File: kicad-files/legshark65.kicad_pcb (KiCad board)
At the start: 2 copper layers, 290 x 92 mm, 158 parts, among them SW1 K2-1187SQ-A4SW-06, SW2 PCM12SMTR, T2 53261-0471, U1 STM32F411CEU6, U3 AT24C256C-SSHL-T, Y1 TAXM8M4RFDCET2T

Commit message: Finished wiring the board
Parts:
- removed SWD1: ~, Legshark:1x02_Long_Header
- added J1: ARM JTAG, acheron_Connectors:PinHeader_2x5_P2.54mm_Vertical, B.Cu at (291.1, 87.4)
- moved Legshark_Logo2 158.7 mm to (83.8, 70.0), turned to -16 degrees
- moved C10 1.63 mm to (259.8, 72.5)
- moved C15 1.60 mm to (246.9, 86.0)
- moved C16 1.27 mm to (246.9, 98.6)
- moved C13 1.21 mm to (261.1, 94.8), turned to 180 degrees
- moved C12 1.11 mm to (261.1, 92.8), turned to 180 degrees
- moved R6 0.54 mm to (246.9, 88.7), turned to 90 degrees
- moved R1 0.15 mm to (247.5, 75.5)
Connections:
- net Net-(U1-BOOT0) renamed BOOT0
- net Net-(U1-NRST) renamed NRST
- net Net-(U1-PB2--BOOT1) renamed BOOT1
- U1 pad 34: Net-(SWD1-SWDIO) -> SWDIO
- U1 pad 37: Net-(SWD1-SWCLK) -> SWCLK
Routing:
- net SWDIO: track 0.00 -> 58.5 mm, vias 0 -> 1
- net BOOT1: track 6.01 -> 62.3 mm, vias 0 -> 1
- net SWCLK: track 0.00 -> 50.7 mm, vias 0 -> 1
- net 3V3: track 88.2 -> 128.9 mm
- net BOOT0: track 28.0 -> 55.2 mm, vias 0 -> 2
- net Net-(SWD1-SWCLK): track 24.7 -> 0.00 mm
- net NRST: track 27.7 -> 47.6 mm, vias 2 -> 3
- net Net-(SWD1-SWDIO): track 19.1 -> 0.00 mm
- net c14: track 100.6 -> 118.6 mm
- net c13: track 89.8 -> 93.4 mm, vias 1 -> 3
- net r4: track 281.7 -> 285.0 mm
- net GND: track 20.5 -> 23.5 mm, vias 12 -> 20
- net c12: track 76.0 -> 78.5 mm
- net c11: track 96.2 -> 98.5 mm
- net c6: track 231.3 -> 229.9 mm
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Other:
- board size 290 x 92 mm -> 286 x 96 mm
- board text added: "3V3"
- board text added: "BOOT0"
- board text added: "BOOT1"
- board text added: "GND"
- board text added: "JTAG"
- board text added: "Reset"
- board text added: "SWCLK"
- board text added: "SWDIO"
- board text added: "nRST"

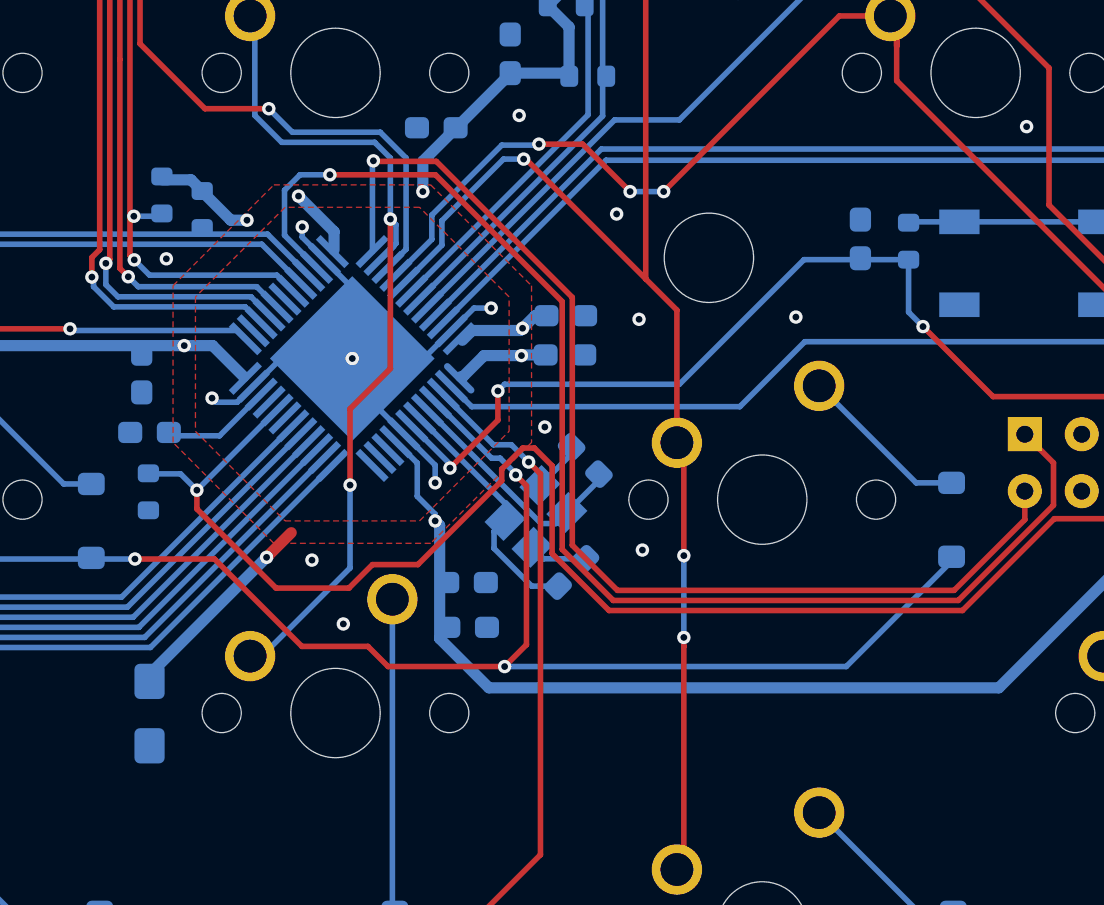
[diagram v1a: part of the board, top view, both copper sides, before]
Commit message: Added names to molex connector
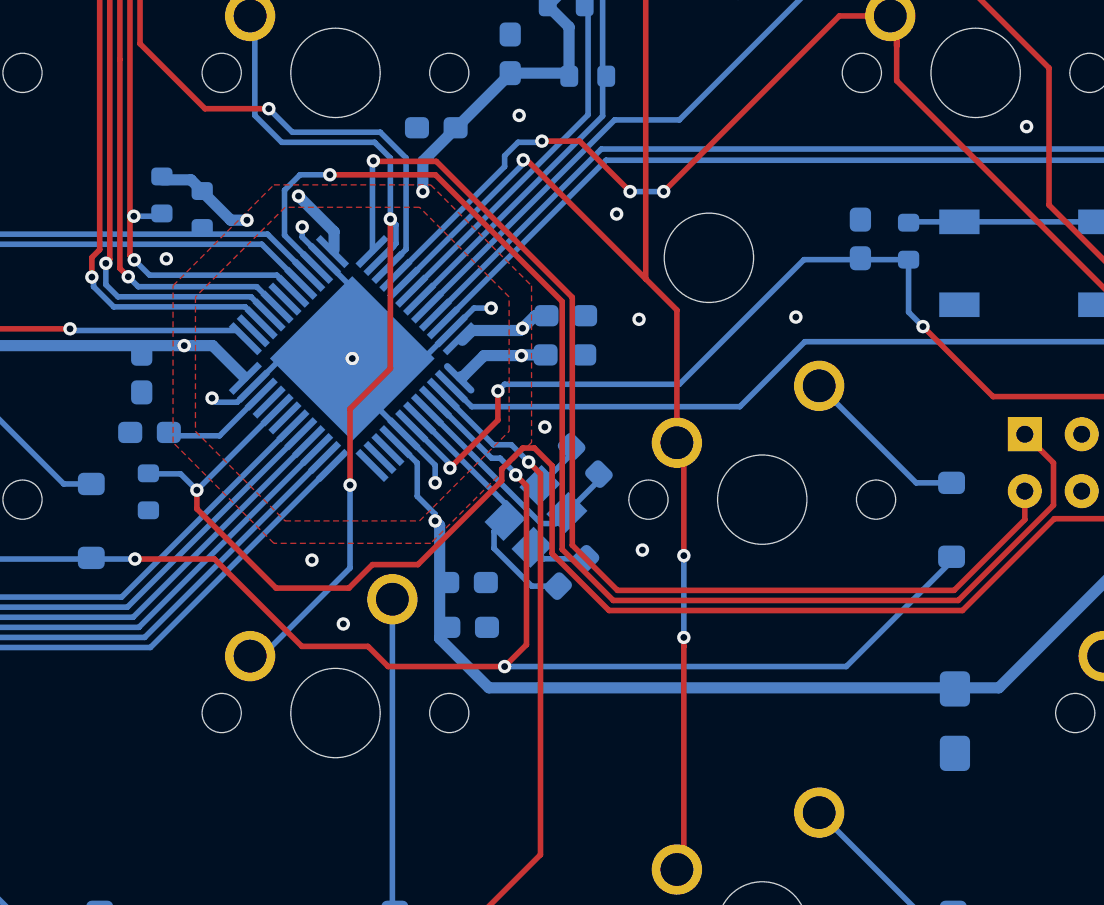
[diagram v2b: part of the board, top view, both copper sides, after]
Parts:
- moved C16 36.0 mm to (282.9, 98.9)
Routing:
- net 3V3: track 128.9 -> 119.6 mm, vias 8 -> 7
- net c13: track 93.4 -> 92.9 mm
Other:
- board text added: "D+"
- board text added: "D-"
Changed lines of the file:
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@@
   )
   (footprint "acheron_Components:CP_EIA-3216-10_Kemet-I_Pad1.58x1.35mm_HandSolder" (layer "B.Cu")
-    (at 246.95 98.6 -90)
+    (at 282.9 98.9375 -90)
     (descr "Tantalum Capacitor SMD Kemet-I (3216-10 Metric), IPC_7351 nominal, (Body size from: http://www.kemet.com/Lists/ProductCatalog/Attachments/253/KEM_TC101_STD.pdf), generated with kicad-footprint-generator")
     (tags "capacitor tantalum")
@@
     (effects (font (size 0.8 0.8) (thickness 0.16)) (justify right mirror))
   )
+  (gr_text "D-" (at 231.3 81) (layer "B.SilkS")
+    (effects (font (size 0.8 0.8) (thickness 0.16)) (justify right mirror))
+  )
   (gr_text "SWCLK" (at 286.02 89.94 90) (layer "B.SilkS")
     (effects (font (size 0.8 0.8) (thickness 0.16)) (justify left mirror))
@@
     (effects (font (size 0.8 0.8) (thickness 0.16)) (justify right mirror))
   )
+  (gr_text "D+" (at 231.3 79.7) (layer "B.SilkS")
+    (effects (font (size 0.8 0.8) (thickness 0.16)) (justify right mirror))
+  )
   (gr_text "3V3" (at 293.64 89.94 90) (layer "B.SilkS")
     (effects (font (size 0.8 0.8) (thickness 0.16)) (justify left mirror))
@@
     (effects (font (size 0.8 0.8) (thickness 0.16)) (justify right mirror))
   )
+  (gr_text "3V3" (at 231.3 82.2) (layer "B.SilkS")
+    (effects (font (size 0.8 0.8) (thickness 0.16)) (justify right mirror))
+  )
   (gr_text "BOOT1" (at 291.1 89.94 90) (layer "B.SilkS")
     (effects (font (size 0.8 0.8) (thickness 0.16)) (justify left mirror))
   )
+  (gr_text "GND" (at 231.3 78.4) (layer "B.SilkS")
+    (effects (font (size 0.8 0.8) (thickness 0.16)) (justify right mirror))
+  )
   (gr_text "GND" (at 296.18 89.94 90) (layer "B.SilkS")
     (effects (font (size 0.8 0.8) (thickness 0.16)) (justify left mirror))
@@
   (segment (start 265.083883 90.118198) (end 265.578858 89.623223) (width 0.25) (layer "B.Cu") (net 3))
   (segment (start 259.358757 85.048097) (end 264.428858 90.118198) (width 0.25) (layer "B.Cu") (net 3))
-  (segment (start 252.175 91.625) (end 253.275 90.525) (width 0.5) (layer "F.Cu") (net 4))
   (via (at 263.6 81.4) (size 0.6) (drill 0.3) (layers "F.Cu" "B.Cu") (net 4))
   (via (at 259.15 75.3) (size 0.6) (drill 0.3) (layers "F.Cu" "B.Cu") (net 4))
@@
   (via (at 259.7 90) (size 0.6) (drill 0.3) (layers "F.Cu" "B.Cu") (net 4))
   (via (at 253.6 75.5) (size 0.6) (drill 0.3) (layers "F.Cu" "B.Cu") (net 4))
-  (via (at 252.175 91.625) (size 0.6) (drill 0.3) (layers "F.Cu" "B.Cu") (net 4))
   (segment (start 263.55 82.62) (end 261.88 82.62) (width 0.5) (layer "B.Cu") (net 4))
   (segment (start 274.1 61.5) (end 277.5 61.5) (width 0.5) (layer "B.Cu") (net 4))
@@
   (segment (start 259.15 75.3) (end 259.15 73.943146) (width 0.5) (layer "B.Cu") (net 4))
   (segment (start 260.936828 83.563172) (end 260.843682 83.563172) (width 0.5) (layer "B.Cu") (net 4))
-  (segment (start 252.175 91.625) (end 246.95 96.85) (width 0.5) (layer "B.Cu") (net 4))
   (segment (start 263.6 81.4) (end 263.5 81.5) (width 0.5) (layer "B.Cu") (net 4))
   (segment (start 255.186828 77.086828) (end 255.186828 77.906318) (width 0.5) (layer "B.Cu") (net 4))
@@
   (segment (start 293.64 88.67) (end 293.64 86.13) (width 0.5) (layer "B.Cu") (net 4))
   (segment (start 269.1 61.9) (end 270.4 60.6) (width 0.5) (layer "B.Cu") (net 4))
-  (segment (start 246.95 96.85) (end 246.95 97.1625) (width 0.5) (layer "B.Cu") (net 4))
   (segment (start 261.88 82.62) (end 260.936828 83.563172) (width 0.5) (layer "B.Cu") (net 4))
   (segment (start 249.3 75.275) (end 248.8 74.775) (width 0.5) (layer "B.Cu") (net 4))
@@
   (segment (start 257.951345 76.77819) (end 257.951345 77.616675) (width 0.25) (layer "B.Cu") (net 88))
   (segment (start 270.8 95.6) (end 270.8 105.25) (width 0.25) (layer "F.Cu") (net 89))
-  (segment (start 263.7495 73.8495) (end 269.1 79.2) (width 0.25) (layer "F.Cu") (net 89))
   (segment (start 270.8 86.82) (end 270.49 86.51) (width 0.25) (layer "F.Cu") (net 89))
+  (segment (start 263.628317 73.884951) (end 263.784951 73.884951) (width 0.25) (layer "F.Cu") (net 89))
+  (segment (start 263.784951 73.884951) (end 269.1 79.2) (width 0.25) (layer "F.Cu") (net 89))
   (segment (start 270.7 60.2) (end 269.1 61.8) (width 0.25) (layer "F.Cu") (net 89))
   (segment (start 270.7 29.57) (end 270.7 60.2) (width 0.25) (layer "F.Cu") (net 89))
   (segment (start 270.49 80.59) (end 270.49 86.51) (width 0.25) (layer "F.Cu") (net 89))
-  (segment (start 263.65 73.8495) (end 263.7495 73.8495) (width 0.25) (layer "F.Cu") (net 89))
   (segment (start 269.1 79.2) (end 270.49 80.59) (width 0.25) (layer "F.Cu") (net 89))
   (segment (start 270.8 91.55) (end 270.8 86.82) (width 0.25) (layer "F.Cu") (net 89))
@@
   (segment (start 269.1 61.8) (end 269.1 79.2) (width 0.25) (layer "F.Cu") (net 89))
   (via (at 270.8 95.2) (size 0.6) (drill 0.3) (layers "F.Cu" "B.Cu") (net 89))
-  (via (at 263.65 73.8495) (size 0.6) (drill 0.3) (layers "F.Cu" "B.Cu") (net 89))
+  (via (at 263.628317 73.884951) (size 0.6) (drill 0.3) (layers "F.Cu" "B.Cu") (net 89))
   (via (at 270.8 91.55) (size 0.6) (drill 0.3) (layers "F.Cu" "B.Cu") (net 89))
-  (segment (start 262.7505 73.8495) (end 260 76.6) (width 0.25) (layer "B.Cu") (net 89))
-  (segment (start 260 76.6) (end 260 77.68934) (width 0.25) (layer "B.Cu") (net 89))
-  (segment (start 260 77.68934) (end 258.298097 79.391243) (width 0.25) (layer "B.Cu") (net 89))
   (segment (start 270.8 95.2) (end 270.8 91.55) (width 0.25) (layer "B.Cu") (net 89))
-  (segment (start 263.65 73.8495) (end 262.7505 73.8495) (width 0.25) (layer "B.Cu") (net 89))
+  (segment (start 263.628317 74.061023) (end 258.298097 79.391243) (width 0.25) (layer "B.Cu") (net 89))
+  (segment (start 263.628317 73.884951) (end 263.628317 74.061023) (width 0.25) (layer "B.Cu") (net 89))
   (segment (start 280.3 67.745) (end 280.3 68.8) (width 0.25) (layer "F.Cu") (net 90))
   (segment (start 297.4 83.25) (end 293.2 83.25) (width 0.25) (layer "F.Cu") (net 90))
@@
   (segment (start 288.59 48.41) (end 289.54 48.41) (width 0.25) (layer "F.Cu") (net 90))
   (segment (start 298.65 84.5) (end 297.4 83.25) (width 0.25) (layer "F.Cu") (net 90))
-  (segment (start 264.331634 73.181634) (end 266.281634 73.181634) (width 0.25) (layer "F.Cu") (net 90))
   (segment (start 289.8 29.44) (end 289.8 48.33) (width 0.25) (layer "F.Cu") (net 90))
   (segment (start 277.74 67.46) (end 280.015 67.46) (width 0.25) (layer "F.Cu") (net 90))
   (segment (start 280.3 68.8) (end 280.3 56.7) (width 0.25) (layer "F.Cu") (net 90))
   (segment (start 289.54 96.035) (end 294.075 91.5) (width 0.25) (layer "F.Cu") (net 90))
-  (segment (start 266.281634 73.181634) (end 268.4 75.3) (width 0.25) (layer "F.Cu") (net 90))
   (segment (start 280.3 56.7) (end 288.59 48.41) (width 0.25) (layer "F.Cu") (net 90))
   (segment (start 289.62 48.33) (end 289.54 48.41) (width 0.25) (layer "F.Cu") (net 90))
@@
   (segment (start 280.015 67.46) (end 280.3 67.745) (width 0.25) (layer "F.Cu") (net 90))
   (segment (start 293.2 83.25) (end 280.3 70.35) (width 0.25) (layer "F.Cu") (net 90))
+  (segment (start 266.147451 73.047451) (end 268.4 75.3) (width 0.25) (layer "F.Cu") (net 90))
+  (segment (start 264.465817 73.047451) (end 266.147451 73.047451) (width 0.25) (layer "F.Cu") (net 90))
   (segment (start 297.2 91.5) (end 298.65 90.05) (width 0.25) (layer "F.Cu") (net 90))
   (segment (start 294.075 91.5) (end 297.2 91.5) (width 0.25) (layer "F.Cu") (net 90))
-  (via (at 264.331634 73.181634) (size 0.6) (drill 0.3) (layers "F.Cu" "B.Cu") (net 90))
+  (via (at 264.465817 73.047451) (size 0.6) (drill 0.3) (layers "F.Cu" "B.Cu") (net 90))
   (via (at 269.9 75.3) (size 0.6) (drill 0.3) (layers "F.Cu" "B.Cu") (net 90))
   (via (at 268.4 75.3) (size 0.6) (drill 0.3) (layers "F.Cu" "B.Cu") (net 90))
-  (segment (start 262.675 73.225) (end 259.55 76.35) (width 0.25) (layer "B.Cu") (net 90))
-  (segment (start 259.55 76.35) (end 259.55 77.432233) (width 0.25) (layer "B.Cu") (net 90))
-  (segment (start 259.55 77.432233) (end 257.944544 79.037689) (width 0.25) (layer "B.Cu") (net 90))
-  (segment (start 264.288268 73.225) (end 262.675 73.225) (width 0.25) (layer "B.Cu") (net 90))
-  (segment (start 264.331634 73.181634) (end 264.288268 73.225) (width 0.25) (layer "B.Cu") (net 90))
+  (segment (start 264.465817 73.047451) (end 264.413268 73.1) (width 0.25) (layer "B.Cu") (net 90))
+  (segment (start 262.8 73.7) (end 262.8 74.182233) (width 0.25) (layer "B.Cu") (net 90))
+  (segment (start 263.4 73.1) (end 262.8 73.7) (width 0.25) (layer "B.Cu") (net 90))
+  (segment (start 264.413268 73.1) (end 263.4 73.1) (width 0.25) (layer "B.Cu") (net 90))
+  (segment (start 262.8 74.182233) (end 257.944544 79.037689) (width 0.25) (layer "B.Cu") (net 90))
   (segment (start 268.4 75.3) (end 269.9 75.3) (width 0.25) (layer "B.Cu") (net 90))
   (segment (start 233.1 77.2) (end 230.625 79.675) (width 0.25) (layer "B.Cu") (net 91))

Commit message: Lost of small changes
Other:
- board text added: "2.25u"
- board text added: "2u"
- board text added: "3u"

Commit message: Fixing up the schematic's of daughter and mother boards
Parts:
- D_0, D_1, D_10, D_11, D_12, D_13, D_14, D_15, D_16, D_17, D_18, D_19, D_2, D_20, D_21, D_22, D_23, D_24, D_25, D_26, D_27, D_28, D_29, D_3, D_30, D_31, D_32, D_33, D_34, D_35, D_36, D_37, D_38, D_39, D_4, D_40, D_41, D_42, D_43, D_44, D_45, D_46, D_47, D_48, D_49, D_5, D_50, D_51, D_52, D_53, D_54, D_55, D_56, D_57, D_58, D_59, D_6, D_60, D_61, D_62, D_63, D_64, D_7, D_8, D_9: value D -> 1N4148W
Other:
- outline, holes or cut-outs redrawn
- rule pad_to_mask_clearance: 0.1 -> 0
